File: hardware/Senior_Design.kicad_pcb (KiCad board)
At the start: 4 copper layers, 142 x 78.1 mm, 147 parts, among them J101 Conn_ARM_JTAG_SWD_10, J201 54-00125, J202 Conn_01x03, J301 Conn_ARM_JTAG_SWD_10, J501 2305018-2, J601 J0011D21BNL, Q201 CSD87503Q3E, Q202 Q_NMOS, Q203 CSD87503Q3E, SW101 SW_Push, SW201 SW_Push, SW301 SW_Push, U101 EFR32FG28A122F1024GM48-A, U201 BQ25798RQMR, U202 TPS63020DSJR, U301 BDE-MB1352P71UA32, U401 TPS613222ADBVR, U402 BME688, U403 USBLC6-2P6, U501 CP2102N-A02-GQFN20, U502 CDSOT236-0504C, U601 W5500, Y101 LF_Crystal, Y102 ECS-390-CDX-1932, Y601 ECS-250-18-5PX-F-TR

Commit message: PCB_layout_1239_Mar10
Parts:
- moved C502 1.01 mm to (157.9, -116.5)
- moved R505 0.31 mm to (167.6, -119.0)
- moved R506 0.21 mm to (172.0, -119.2)
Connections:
- U202 pad 16: (no net) -> GND
- U202 pad 17: (no net) -> GND
- U202 pad 18: (no net) -> GND
- U202 pad 19: (no net) -> GND
- U202 pad 20: (no net) -> GND
- U202 pad 21: (no net) -> GND
- U202 pad 23: (no net) -> GND
- U202 pad 24: (no net) -> GND
- U202 pad 25: (no net) -> GND
- U202 pad 26: (no net) -> GND
- U202 pad 27: (no net) -> GND
- U202 pad 28: (no net) -> GND
- U202 pad 29: (no net) -> GND
- U202 pad 30: (no net) -> GND
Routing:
- net /BME 688 and SPS30/SCL: track 55.1 -> 52.7 mm
- net Net-(Q202-G): track 13.6 -> 12.1 mm
- net Net-(C614-Pad1): track 12.0 -> 10.7 mm
- net Net-(U601-XO): track 22.5 -> 21.9 mm
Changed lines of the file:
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@@
 	(footprint "Capacitor_SMD:C_0805_2012Metric"
 		(layer "F.Cu")
-		(at 158.875 -116.775 -90)
+		(at 157.9 -116.5 -90)
 		(descr "Capacitor SMD 0805 (2012 Metric), square (rectangular) end terminal, IPC-7351 nominal, (Body size source: IPC-SM-782 page 76, https://www.pcb-3d.com/wordpress/wp-content/uploads/ipc-sm-782a_amendment_1_and_2.pdf, https://docs.google.com/spreadsheets/d/1BsfQQcO9C6DZCsRaXUlFlo91Tg2WpOkGARC1WS5S8t0/edit?usp=sharing), generated with kicad-footprint-generator")
 		(tags "capacitor")
@@
 	(footprint "Resistor_SMD:R_0805_2012Metric"
 		(layer "F.Cu")
-		(at 172 -119.3625 90)
+		(at 172 -119.15 90)
 		(descr "Resistor SMD 0805 (2012 Metric), square (rectangular) end terminal, IPC-7351 nominal, (Body size source: IPC-SM-782 page 72, https://www.pcb-3d.com/wordpress/wp-content/uploads/ipc-sm-782a_amendment_1_and_2.pdf), generated with kicad-footprint-generator")
 		(tags "resistor")
@@
 			(layers "*.Cu" "*.Mask")
 			(remove_unused_layers no)
+			(net 1 "GND")
 			(solder_mask_margin 0.102)
 		)
@@
 			(layers "*.Cu" "*.Mask")
 			(remove_unused_layers no)
+			(net 1 "GND")
 			(solder_mask_margin 0.102)
 		)
@@
 			(layers "*.Cu" "*.Mask")
 			(remove_unused_layers no)
+			(net 1 "GND")
 			(solder_mask_margin 0.102)
 		)
@@
 			(layers "*.Cu" "*.Mask")
 			(remove_unused_layers no)
+			(net 1 "GND")
 			(solder_mask_margin 0.102)
 		)
@@
 			(layers "*.Cu" "*.Mask")
 			(remove_unused_layers no)
+			(net 1 "GND")
 			(solder_mask_margin 0.102)
 		)
@@
 			(layers "*.Cu" "*.Mask")
 			(remove_unused_layers no)
-			(solder_mask_margin 0.102)
-		)
-		(pad "22" thru_hole circle
-			(at -0.5 0 180)
-			(size 0.3 0.3)
-			(drill 0.2)
-			(layers "*.Cu" "*.Mask")
-			(remove_unused_layers no)
+			(net 1 "GND")
 			(solder_mask_margin 0.102)
 		)
@@
 			(layers "*.Cu" "*.Mask")
 			(remove_unused_layers no)
+			(net 1 "GND")
 			(solder_mask_margin 0.102)
 		)
@@
 			(layers "*.Cu" "*.Mask")
 			(remove_unused_layers no)
+			(net 1 "GND")
 			(solder_mask_margin 0.102)
 		)
@@
 			(layers "*.Cu" "*.Mask")
 			(remove_unused_layers no)
+			(net 1 "GND")
 			(solder_mask_margin 0.102)
 		)
@@
 			(layers "*.Cu" "*.Mask")
 			(remove_unused_layers no)
+			(net 1 "GND")
 			(solder_mask_margin 0.102)
 		)
@@
 			(layers "*.Cu" "*.Mask")
 			(remove_unused_layers no)
+			(net 1 "GND")
 			(solder_mask_margin 0.102)
 		)
@@
 			(layers "*.Cu" "*.Mask")
 			(remove_unused_layers no)
+			(net 1 "GND")
 			(solder_mask_margin 0.102)
 		)
@@
 			(layers "*.Cu" "*.Mask")
 			(remove_unused_layers no)
+			(net 1 "GND")
 			(solder_mask_margin 0.102)
 		)
@@
 			(layers "*.Cu" "*.Mask")
 			(remove_unused_layers no)
+			(net 1 "GND")
+			(solder_mask_margin 0.102)
+		)
+		(pad "gnd" thru_hole circle
+			(at -0.5 0 180)
+			(size 0.3 0.3)
+			(drill 0.2)
+			(layers "*.Cu" "*.Mask")
+			(remove_unused_layers no)
+			(net 1 "GND")
 			(solder_mask_margin 0.102)
 		)
@@
 	(footprint "Resistor_SMD:R_0805_2012Metric"
 		(layer "F.Cu")
-		(at 167.625 -119.3125 90)
+		(at 167.6 -119 90)
 		(descr "Resistor SMD 0805 (2012 Metric), square (rectangular) end terminal, IPC-7351 nominal, (Body size source: IPC-SM-782 page 72, https://www.pcb-3d.com/wordpress/wp-content/uploads/ipc-sm-782a_amendment_1_and_2.pdf), generated with kicad-footprint-generator")
 		(tags "resistor")
@@
 		(tags "SOD-123")
 		(property "Reference" "D201"
-			(at -0.15 -2 90)
+			(at 3.058 0.025 180)
 			(layer "B.SilkS")
 			(effects
@@
 		(at 70.875 -101.9195)
 		(property "Reference" "Q201"
-			(at 0.82408 2.63582 0)
+			(at -2.425 3.3695 0)
 			(layer "B.SilkS")
 			(effects
@@
 		(tags "resistor")
 		(property "Reference" "R201"
-			(at -0.0125 -1.6 90)
+			(at -0.882 -1.925 90)
 			(layer "B.SilkS")
 			(effects
@@
 	)
 	(segment
-		(start 89.738 -100.279)
-		(end 90.238 -100.779)
-		(width 0.16)
-		(layer "F.Cu")
-		(net 1)
-	)
-	(segment
 		(start 74 -109)
 		(end 80.6 -109)
@@
 	)
 	(segment
-		(start 89.063 -100.279)
-		(end 89.738 -100.279)
-		(width 0.16)
-		(layer "F.Cu")
-		(net 1)
-	)
-	(segment
-		(start 90.238 -100.779)
-		(end 90.238 -102.379)
-		(width 0.16)
-		(layer "F.Cu")
-		(net 1)
-	)
-	(segment
 		(start 79.5 -102.6)
 		(end 75 -102.6)
@@
 	)
 	(segment
+		(start 89.063 -100.279)
+		(end 89.063 -100.313)
+		(width 0.16)
+		(layer "F.Cu")
+		(net 1)
+	)
+	(segment
+		(start 90.238 -101.488)
+		(end 90.238 -102.379)
+		(width 0.16)
+		(layer "F.Cu")
+		(net 1)
+	)
+	(segment
 		(start 82.821 -105.779)
 		(end 83.55 -105.779)
@@
 		(net 1)
 	)
+	(segment
+		(start 89.063 -100.313)
+		(end 90.238 -101.488)
+		(width 0.16)
+		(layer "F.Cu")
+		(net 1)
+	)
 	(via blind
 		(at 84.21545 -63.47645)
@@
 	)
 	(segment
-		(start 38.36 -82.035)
-		(end 38.36 -79.635)
-		(width 0.12)
-		(layer "F.Cu")
-		(net 16)
-	)
-	(segment
 		(start 88.177497 -85.152441)
 		(end 92.375522 -80.954416)
@@
 	)
 	(segment
-		(start 132.6853 -78.0504)
-		(end 133.6853 -77.0504)
+		(start 131.6853 -78.0504)
+		(end 131.6996 -78.0504)
 		(width 0.2)
 		(layer "F.Cu")
@@
 	)
 	(segment
-		(start 132.6853 -69.0504)
-		(end 131.5103 -69.0504)
+		(start 131.6996 -78.0504)
+		(end 133.6853 -76.0647)
 		(width 0.2)
 		(layer "F.Cu")
@@
 	)
 	(segment
-		(start 133.6853 -73.5504)
-		(end 133.6853 -70.0504)
+		(start 133.6853 -76.0647)
+		(end 133.6853 -73.5504)
 		(width 0.2)
 		(layer "F.Cu")
@@
 	)
 	(segment
-		(start 131.6853 -78.0504)
-		(end 132.6853 -78.0504)
+		(start 133.6853 -73.5504)
+		(end 133.6853 -71.2353)
 		(width 0.2)
 		(layer "F.Cu")
@@
 	)
 	(segment
-		(start 133.6853 -77.0504)
-		(end 133.6853 -73.5504)
+		(start 133.6853 -71.2353)
+		(end 131.5103 -69.0603)
 		(width 0.2)
 		(layer "F.Cu")
@@
 	)
 	(segment
-		(start 133.6853 -70.0504)
-		(end 132.6853 -69.0504)
+		(start 131.5103 -69.0603)
+		(end 131.5103 -69.0504)
 		(width 0.2)
 		(layer "F.Cu")
@@
 	)
 	(segment
-		(start 124.6853 -78.0504)
-		(end 125.7853 -78.0504)
+		(start 124.1853 -73.5504)
+		(end 124.1853 -76.4853)
 		(width 0.12)
 		(layer "F.Cu")
@@
 	)
 	(segment
-		(start 124.1853 -77.5504)
-		(end 124.6853 -78.0504)
-		(width 0.12)
+		(start 129.9353 -60.4629)
+		(end 125.6853 -64.7129)
+		(width 0.2)
 		(layer "F.Cu")
 		(net 25)
 	)
 	(segment
-		(start 124.1853 -73.5504)
-		(end 124.1853 -77.5504)
+		(start 125.7504 -78.0504)
+		(end 125.7853 -78.0504)
 		(width 0.12)
 		(layer "F.Cu")
@@
 	)
 	(segment
-		(start 129.9353 -60.4629)
-		(end 125.6853 -64.7129)
-		(width 0.2)
+		(start 124.1853 -76.4853)
+		(end 125.7504 -78.0504)
+		(width 0.12)
 		(layer "F.Cu")
 		(net 25)
@@
 	)
 	(segment
-		(start 172 -118.45)
-		(end 172 -115.93075)
+		(start 172.2 -106.85)
+		(end 172.4 -107.05)
 		(width 0.2)
 		(layer "F.Cu")
@@
 	)
 	(segment
-		(start 172 -115.93075)
-		(end 172.1625 -115.76825)
+		(start 175.4 -115.65)
+		(end 172.3 -115.65)
 		(width 0.2)
 		(layer "F.Cu")
@@
 	)
 	(segment
-		(start 172.2 -106.85)
-		(end 172.4 -107.05)
+		(start 172.3 -115.65)
+		(end 172.2 -115.75)
 		(width 0.2)
 		(layer "F.Cu")
@@
 	)
 	(segment
-		(start 175.4 -115.65)
-		(end 172.3 -115.65)
+		(start 172 -118.2375)
+		(end 172 -115.93075)
 		(width 0.2)
 		(layer "F.Cu")
@@
 	)
 	(segment
-		(start 172.3 -115.65)
-		(end 172.2 -115.75)
+		(start 175.4 -107.05)
+		(end 175.4 -115.65)
 		(width 0.2)
 		(layer "F.Cu")
@@
 	)
 	(segment
-		(start 175.4 -107.05)
-		(end 175.4 -115.65)
+		(start 172 -115.93075)
+		(end 172.1625 -115.76825)
 		(width 0.2)
 		(layer "F.Cu")
@@
 	)
 	(segment
-		(start 85.3625 -104.5)
-		(end 86.5 -104.5)
+		(start 87.55 -105.55)
+		(end 92.5 -105.55)
 		(width 0.16)
 		(layer "F.Cu")
@@
 	)
 	(segment
-		(start 86.5 -104.5)
-		(end 87.55 -105.55)
+		(start 95.721 -102.329)
+		(end 95.738 -102.329)
 		(width 0.16)
 		(layer "F.Cu")
@@
 	)
 	(segment
-		(start 87.55 -105.55)
-		(end 95.05 -105.55)
+		(start 86.5 -104.5)
+		(end 87.55 -105.55)
 		(width 0.16)
 		(layer "F.Cu")
@@
 	)
 	(segment
-		(start 95.05 -105.55)
-		(end 95.738 -104.862)
+		(start 85.3625 -104.5)
+		(end 86.5 -104.5)
 		(width 0.16)
 		(layer "F.Cu")
@@
 	)
 	(segment
-		(start 95.738 -104.862)
-		(end 95.738 -102.329)
+		(start 92.5 -105.55)
+		(end 95.721 -102.329)
 		(width 0.16)
 		(layer "F.Cu")

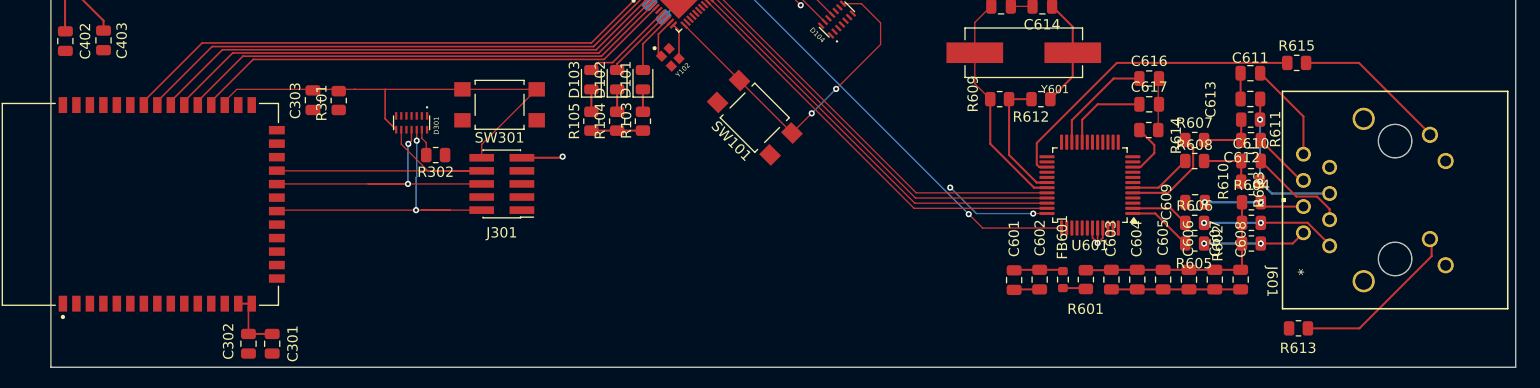
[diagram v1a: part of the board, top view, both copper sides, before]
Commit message: ethernet/wisun pcb update
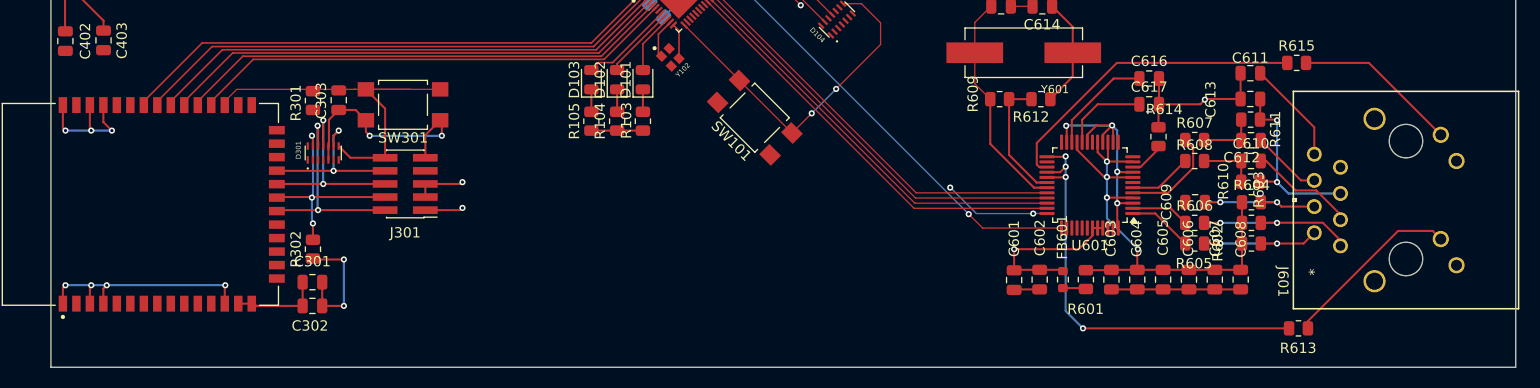
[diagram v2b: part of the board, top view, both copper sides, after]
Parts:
- moved R302 15.0 mm to (60.0, -54.5), turned to 90 degrees
- moved J301 9.37 mm to (69.0, -60.8)
- moved SW301 9.37 mm to (68.7, -68.5)
- moved D301 9.05 mm to (61.0, -63.8), turned to 90 degrees
- moved C302 7.21 mm to (60.0, -49.0), turned to 180 degrees
- moved C301 7.13 mm to (60.0, -51.3), turned to 180 degrees
- moved C303 2.50 mm to (62.5, -69.0)
- moved R301 2.50 mm to (60.0, -68.9)
- moved R614 1.14 mm to (142.0, -65.4), turned to 90 degrees
- moved J601 1.05 mm to (159.7, -54.8)
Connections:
- U202 pad 16: GND -> (no net)
- U202 pad 17: GND -> (no net)
- U202 pad 18: GND -> (no net)
- U202 pad 19: GND -> (no net)
- U202 pad 20: GND -> (no net)
- U202 pad 21: GND -> (no net)
- U202 pad 23: GND -> (no net)
- U202 pad 24: GND -> (no net)
- U202 pad 25: GND -> (no net)
- U202 pad 26: GND -> (no net)
- U202 pad 27: GND -> (no net)
- U202 pad 28: GND -> (no net)
- U202 pad 29: GND -> (no net)
- U202 pad 30: GND -> (no net)
- U202 pad gnd: GND -> (no net)
- U601 pad 23: unconnected-(U601-RSVD-Pad23) -> GND
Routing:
- net GND: track 115.5 -> 210.8 mm, vias 3 -> 18
- net /Ethernet/LINKLED: track 0.00 -> 39.2 mm, vias 0 -> 2
- net +3.3VA: track 22.0 -> 50.2 mm, vias 0 -> 4
- net +3.3V: track 23.8 -> 48.6 mm, vias 1 -> 5
- net /Wi-SUN Module/JTAG_TCKC: track 2.64 -> 21.8 mm, vias 0 -> 3
- net /Wi-SUN Module/JTAG_TDI: track 30.2 -> 16.3 mm, vias 0 -> 2
- net /Wi-SUN Module/JTAG_TDO: track 29.1 -> 19.2 mm
- net /Wi-SUN Module/JTAG_TMSC: track 30.5 -> 20.7 mm
- net /MCU/BDE_RST: track 44.4 -> 38.6 mm
- net Net-(C613-Pad1): track 14.7 -> 18.0 mm
- net /Ethernet/TD+: track 13.2 -> 16.1 mm
- net Net-(C609-Pad1): track 9.73 -> 12.4 mm
- net /Ethernet/TD-: track 10.1 -> 12.7 mm
- net Net-(U601-EXRES1): track 5.48 -> 3.50 mm
- net VDD: track 7.01 -> 8.63 mm
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
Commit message: PCB WIP
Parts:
- moved C614 140.6 mm to (24.4, 14.0), turned to 0 degrees
- moved C615 134.7 mm to (28.4, 14.0), turned to 180 degrees
- moved Y601 132.1 mm to (26.2, 9.50), turned to 0 degrees
- moved R612 129.3 mm to (24.6, 5.00), turned to 180 degrees
- moved R609 122.8 mm to (28.6, 5.00), turned to 0 degrees
- moved J501 119.4 mm to (79.0, -41.1)
- moved R502 119.4 mm to (65.6, -46.8)
- moved R504 119.4 mm to (69.7, -37.0)
- moved C501 119.4 mm to (56.6, -47.1)
- moved C502 119.4 mm to (61.3, -46.3)
- moved D501 119.4 mm to (72.6, -29.9)
- moved D503 119.4 mm to (60.7, -36.2)
- moved R501 119.4 mm to (68.8, -30.9)
- moved R503 119.4 mm to (66.5, -29.1)
- moved R505 119.4 mm to (71.0, -48.8)
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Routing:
- net /Ethernet/W5500_RST: track 48.4 -> 2.54 mm, vias 2 -> 1
- net /BME 688 and SPS30/SCL: track 52.7 -> 23.7 mm
- net /BME 688 and SPS30/SDA: track 52.3 -> 23.5 mm
- net /Ethernet/SPI_SCK: track 40.5 -> 13.3 mm
- net /Ethernet/SPI_MOSI: track 41.2 -> 14.1 mm
- net /Ethernet/SPI_MISO: track 40.8 -> 13.7 mm
- net /Ethernet/SPI_CS: track 40.1 -> 12.9 mm
- net /MCU/MCU_TX_CP_RX: track 73.4 -> 47.7 mm, vias 1 -> 0
- net /MCU/MCU_RX_CP_TX: track 74.1 -> 48.4 mm, vias 1 -> 0
- net /MCU/MCU_TX_BDE_RX: track 51.8 -> 41.3 mm
- net /MCU/BDE_DEBUG0: track 48.4 -> 37.9 mm
- net /MCU/BDE_DEBUG1: track 47.3 -> 36.8 mm
- net /MCU/MCU_CTS_BDE_RTS: track 49.5 -> 39.1 mm
- net /Ethernet/W5500_INT: track 11.1 -> 0.67 mm, vias 2 -> 0
- net /MCU/MCU_RX_BDE_TX: track 53.0 -> 42.5 mm
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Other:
- board size 142 x 78.1 mm -> 111.5 x 73.6 mm

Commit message: PCB_layout_2225_Mar10
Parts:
- C301, C302: moved to B.Cu
- moved C402 32.1 mm to (-24.6, -13.0)
- moved C403 32.1 mm to (-20.9, -13.0)
- moved U402 32.1 mm to (-23.4, -19.1)
- moved R102 29.4 mm to (-24.9, -25.8)
- moved U403 20.2 mm to (-33.4, -40.0)
- moved D401 20.2 mm to (-38.0, -35.0)
- moved SPS30_Connector401 20.2 mm to (-43.2, -47.0)
- moved L401 20.2 mm to (-22.7, -33.4)
- moved U401 20.2 mm to (-22.5, -36.9)
- moved C401 20.2 mm to (-22.8, -40.0)
- moved R101 15.2 mm to (-38.1, -22.9)
- moved C302 7.25 mm to (-10.3, 14.8), turned to 90 degrees
- moved C301 5.63 mm to (-8.20, 14.8), turned to 90 degrees
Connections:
- U202 pad 16: (no net) -> GND
- U202 pad 17: (no net) -> GND
- U202 pad 18: (no net) -> GND
- U202 pad 19: (no net) -> GND
- U202 pad 20: (no net) -> GND
- U202 pad 21: (no net) -> GND
- U202 pad 23: (no net) -> GND
- U202 pad 24: (no net) -> GND
- U202 pad 25: (no net) -> GND
- U202 pad 26: (no net) -> GND
- U202 pad 27: (no net) -> GND
- U202 pad 28: (no net) -> GND
- U202 pad 29: (no net) -> GND
- U202 pad 30: (no net) -> GND
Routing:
- net +3.3V: track 48.6 -> 36.8 mm, vias 5 -> 3
- net VDD: track 8.63 -> 3.16 mm, vias 0 -> 1

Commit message: Power Layout WIP
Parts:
- removed the C611 at (56.7, -14.1)
- C201, C202, C222, C223, C224, C225, C226, C227: footprint Capacitor_SMD:C_0805_2012Metric -> Capacitor_SMD:C_0603_1608Metric
- C206, C208, C211, C212, C221: footprint Capacitor_SMD:C_0805_2012Metric -> Capacitor_SMD:C_0402_1005Metric
- C210: footprint Capacitor_SMD:C_0805_2012Metric -> Capacitor_SMD:C_0603_1608Metric; moved to F.Cu
- D201, Q201, R201, R202, R207, R208: moved to F.Cu
- R211, R213: footprint Resistor_SMD:R_0805_2012Metric -> Resistor_SMD:R_0603_1608Metric
- moved C227 52.8 mm to (69.8, -64.9), turned to 0 degrees
- moved R211 49.9 mm to (74.4, -66.4), turned to 180 degrees
- moved C203 49.6 mm to (24.3, -70.8)
- moved D202 49.6 mm to (25.5, -74.0)
- moved C225 49.1 mm to (61.4, -68.9)
- moved L202 48.7 mm to (67.6, -74.5)
- moved C226 48.5 mm to (63.0, -68.9)
- moved C223 48.1 mm to (72.0, -68.9)
- moved U202 48.1 mm to (67.5, -67.9)
- moved C224 47.7 mm to (73.6, -68.9)
- moved C222 47.2 mm to (75.2, -68.9)
- moved R213 45.1 mm to (72.1, -65.7), turned to -90 degrees
- moved J202 43.1 mm to (45.5, -84.5)
- moved Q203 41.7 mm to (22.3, -67.2)
- moved R204 41.7 mm to (28.0, -66.7)
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- renumbered C612 to C611, C613 to C612, C614 to C613, C615 to C614, C616 to C615, C617 to C616, R602 to R601, R603 to R602, R604 to R603, R605 to R604, R606 to R605, R607 to R606, R608 to R607, R601 to R608
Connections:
- FB601 pad 2: Net-(FB601-Pad2) -> +3.3VA
- J601 pad 8: Net-(C611-Pad1) (its old number) -> Net-(J601-Pad8)
- R608 pad 1: +3.3VA -> Net-(J601-Pad8)
- R608 pad 2: Net-(FB601-Pad2) -> GND
- U202 pad 16: GND -> (no net)
- U202 pad 17: GND -> (no net)
- U202 pad 18: GND -> (no net)
- U202 pad 19: GND -> (no net)
- U202 pad 20: GND -> (no net)
- U202 pad 21: GND -> (no net)
- U202 pad 22: GND -> (no net)
- U202 pad 23: GND -> (no net)
- U202 pad 24: GND -> (no net)
- U202 pad 25: GND -> (no net)
- U202 pad 26: GND -> (no net)
- U202 pad 27: GND -> (no net)
- U202 pad 28: GND -> (no net)
- U202 pad 29: GND -> (no net)
- U202 pad 30: GND -> (no net)
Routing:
- net GND: track 211.9 -> 179.6 mm, vias 17 -> 42
- net /BMS/TS: track 30.0 -> 0.00 mm, vias 1 -> 0
- net /BMS/VAC2: track 31.7 -> 1.94 mm
- net Net-(J202-Pin_1): track 28.4 -> 0.00 mm, vias 1 -> 0
- net /BMS/QON: track 37.4 -> 10.0 mm, vias 2 -> 0
- net /BMS/BQ_INT: track 28.4 -> 12.0 mm, vias 2 -> 1
- net /BMS/REGN: track 22.2 -> 6.14 mm, vias 3 -> 0
- net /BMS/ACDRV1: track 15.1 -> 0.96 mm, vias 2 -> 0
- net +3.3V: track 36.8 -> 23.3 mm
- net /BMS/PS_SYNC: track 22.3 -> 9.69 mm, vias 2 -> 1
- net Net-(C204-Pad1): track 16.8 -> 4.89 mm, vias 1 -> 0
- net /BME 688 and SPS30/SCL: track 23.7 -> 12.6 mm
- net /BME 688 and SPS30/SDA: track 23.5 -> 12.5 mm
- net /BMS/SYS: track 23.6 -> 13.0 mm
- net Net-(Q202-G): track 12.1 -> 1.71 mm, vias 0 -> 1
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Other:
- board size 111.5 x 73.6 mm -> 135.6 x 132 mm

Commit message: PCB_layout_1215_Mar11
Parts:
- C108, C109: moved to F.Cu
- C402, C403, C501, C502, C601, C602, C603, C604, C605, C606, C607, C608, R505: moved to B.Cu
- moved C106 23.7 mm to (21.7, -11.6), turned to -135 degrees
- moved C102 22.8 mm to (25.6, -12.6), turned to 45 degrees
- moved C107 22.4 mm to (20.0, -14.2), turned to -135 degrees
- moved R503 20.8 mm to (61.4, -49.2), turned to 90 degrees
- moved C108 20.8 mm to (22.5, -16.6), turned to 45 degrees
- moved C109 20.0 mm to (21.1, -18.1), turned to 45 degrees
- moved C101 19.7 mm to (24.1, -14.0), turned to 45 degrees
- moved R501 18.7 mm to (64.7, -49.2)
- moved D501 17.7 mm to (69.5, -47.2), turned to 90 degrees
- moved C103 16.2 mm to (23.5, -16.2), turned to 45 degrees
- moved C104 15.8 mm to (22.0, -17.7), turned to 45 degrees
- moved C605 14.2 mm to (41.4, -6.55), turned to 90 degrees
- moved C603 13.4 mm to (44.6, -7.40), turned to 0 degrees
- moved C606 12.9 mm to (44.6, -5.40), turned to 0 degrees
- moved C607 12.7 mm to (44.6, -3.35), turned to 0 degrees
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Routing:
- net GND: track 179.6 -> 136.7 mm
- net +3.3V: track 23.3 -> 65.8 mm
- net USB_VBUS: track 27.7 -> 68.1 mm, vias 3 -> 0
- net /MCU/JTAG_TCK: track 10.9 -> 36.7 mm, vias 2 -> 3
- net /MCU/JTAG_TDI: track 10.6 -> 36.2 mm
- net /MCU/nRST: track 24.8 -> 49.6 mm, vias 3 -> 4
- net /MCU/JTAG_TDO: track 10.8 -> 34.3 mm, vias 2 -> 3
- net /MCU/JTAG_TMS: track 13.5 -> 36.8 mm, vias 2 -> 3
- net +3.3VA: track 52.5 -> 65.3 mm
- net Net-(U501-VBUS): track 20.6 -> 8.27 mm, vias 2 -> 0
- net /MCU/DVDD: track 8.09 -> 0.48 mm, vias 1 -> 0
- net /USB-C/CC1: track 10.1 -> 3.22 mm
- net /MCU/MCU_RX_CP_TX: track 48.4 -> 42.1 mm
- net /MCU/MCU_TX_CP_RX: track 47.7 -> 42.0 mm
- net /USB-C/D_N: track 15.5 -> 20.3 mm, vias 0 -> 2
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
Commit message: 5VB PCB layout
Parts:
- added C401: 10uF, Capacitor_SMD:C_0402_1005Metric, F.Cu at (-24.3, -42.0)
- added C403: 10uF, Capacitor_SMD:C_0603_1608Metric, F.Cu at (-24.3, -52.4)
- added C404: 10uF, Capacitor_SMD:C_0603_1608Metric, F.Cu at (-24.3, -50.9)
- added C405: 2.2uF, Capacitor_SMD:C_0603_1608Metric, F.Cu at (-27.3, -49.4)
- added D401: D_Schottky, Diode_SMD:D_0805_2012Metric, F.Cu at (-24.9, -43.5)
- added R401: R, Resistor_SMD:R_0402_1005Metric, F.Cu at (-25.4, -41.0)
- C402: renamed from C401; value 22uF -> 10uF; footprint Capacitor_SMD:C_0805_2012Metric -> Capacitor_SMD:C_0603_1608Metric
- C406: renamed from C402; moved to F.Cu
- C407: renamed from C403; moved to F.Cu
- L401: footprint Inductor_SMD:L_1210_3225Metric -> Inductor_SMD:L_1008_2520Metric
- moved C203 53.4 mm to (-29.1, -68.0)
- moved D202 50.6 mm to (-25.0, -71.0)
- moved Q201 49.1 mm to (-31.3, -70.8)
- moved D201 40.9 mm to (-27.0, -63.9)
- moved D204 36.4 mm to (-9.00, -49.9), turned to -90 degrees
- moved R205 36.2 mm to (-6.50, -49.9)
- moved R201 35.9 mm to (-25.0, -67.1)
- moved R206 29.2 mm to (30.0, -39.6)
- moved D203 24.0 mm to (34.6, -42.0)
- moved R101 23.3 mm to (-15.4, -18.0)
- moved R210 22.8 mm to (8.50, -45.9)
- moved Q203 22.0 mm to (31.1, -47.1)
- moved C207 21.8 mm to (34.0, -46.5)
- moved R204 21.7 mm to (36.0, -46.5)
- moved C209 21.2 mm to (39.0, -46.5)
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- renumbered D401 to D402
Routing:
- net USB_VBUS: track 68.1 -> 24.2 mm
- net +5V: track 25.2 -> 8.81 mm
- net Net-(U402-VDDIO): track 3.71 -> 0.00 mm, vias 1 -> 0
- net Net-(U402-VDD): track 3.19 -> 0.00 mm, vias 1 -> 0
- net Net-(D401-A): track 2.64 -> 0.00 mm
- net /BMS/TS: track 0.00 -> 1.22 mm
